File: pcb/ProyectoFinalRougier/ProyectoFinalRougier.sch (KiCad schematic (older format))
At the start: 24 parts, among them J1 Screw_Terminal_01x02, J2 Conn_01x06, J3 Screw_Terminal_01x02, U1 AD8495, U2 TL431DBZ, U3 AD8495, U4 TL431DBZ

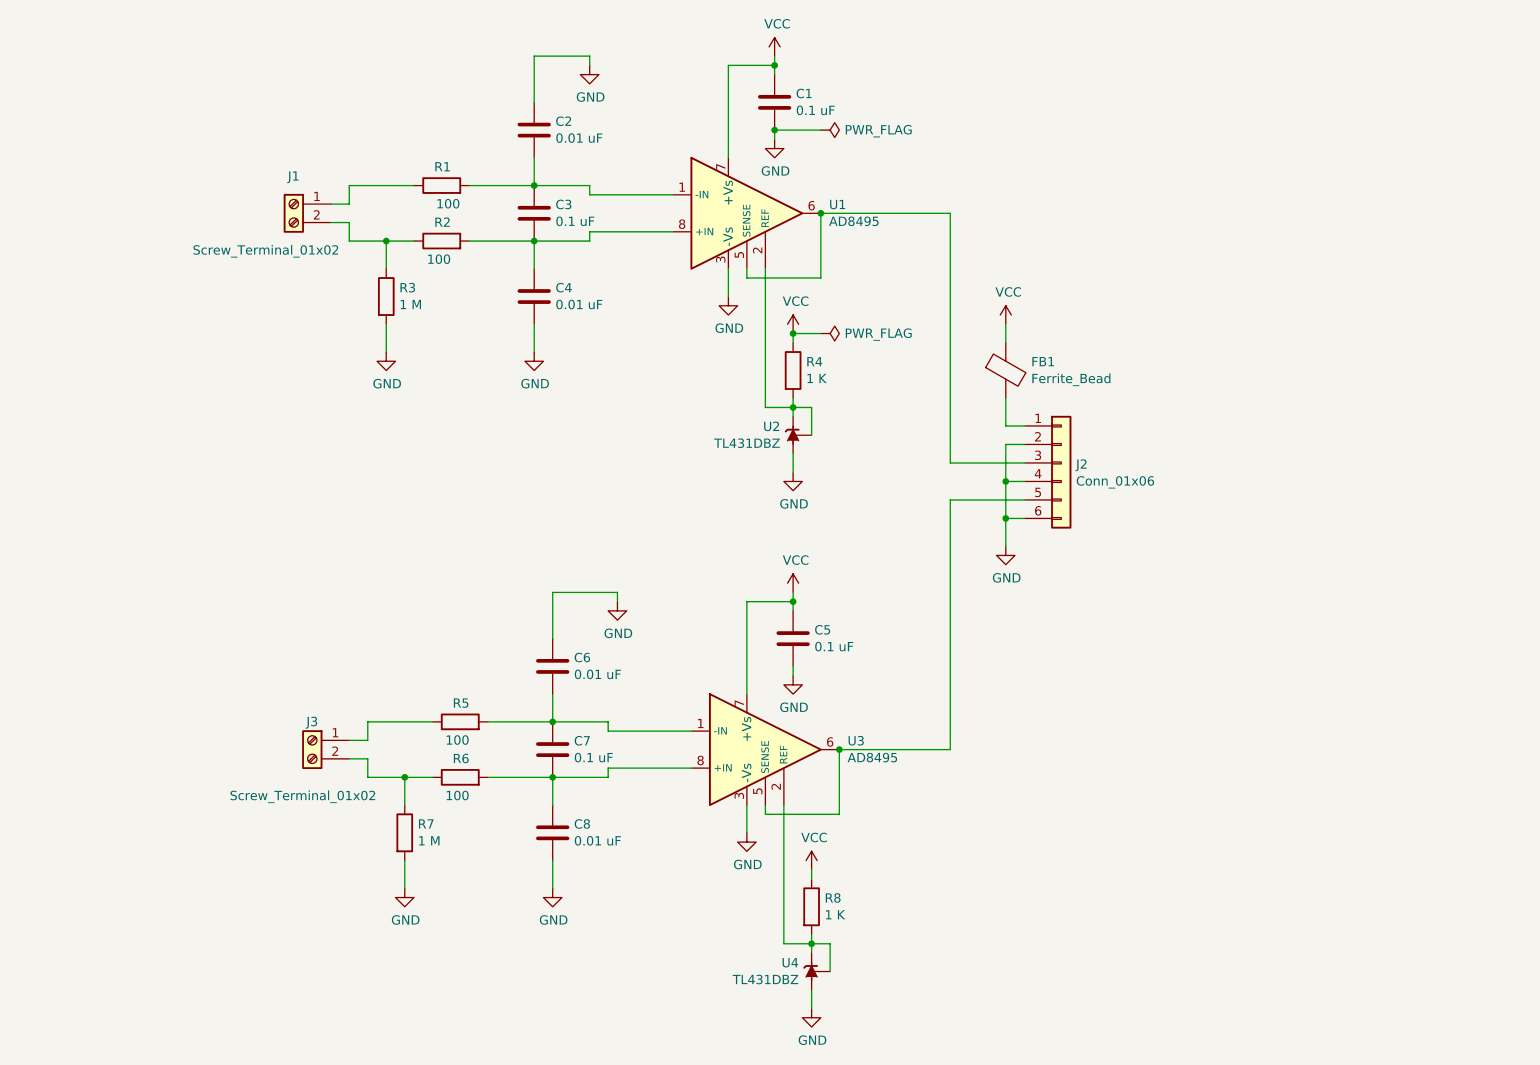
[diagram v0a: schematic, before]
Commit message: Se agregan Fiduciales y Mounting hole, se corrige ubicación de algunos componentes
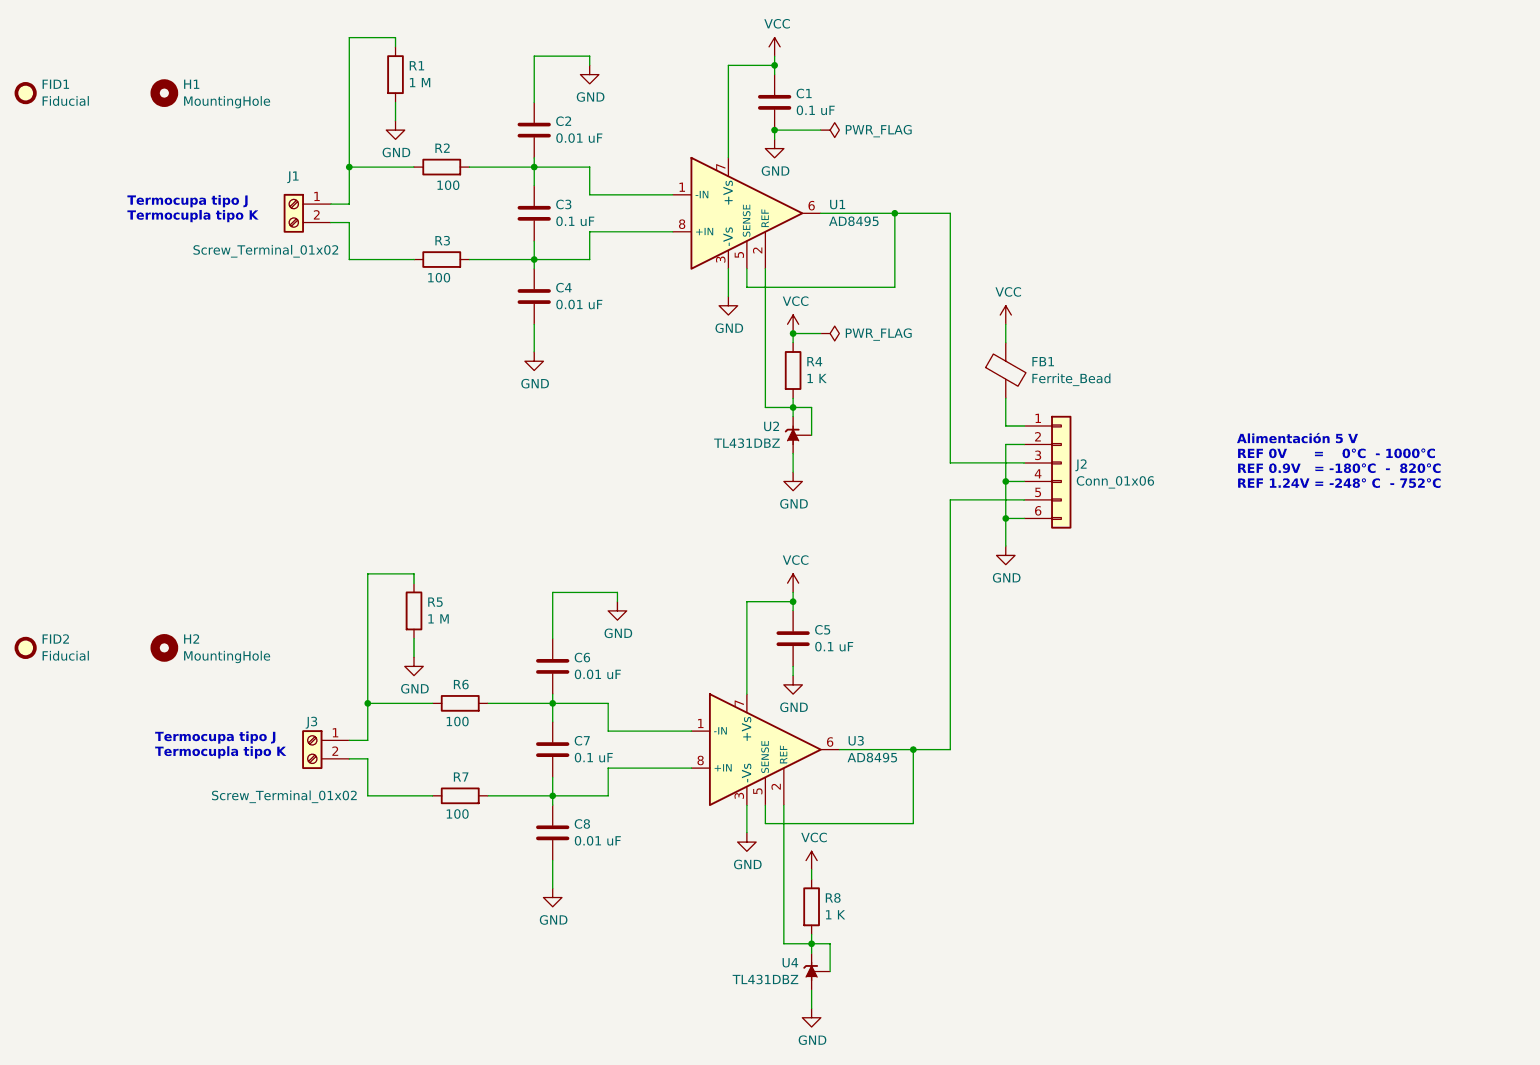
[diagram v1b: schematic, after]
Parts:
- added FID1, FID2: Fiducial, Fiducial:Fiducial_0.75mm_Mask2.25mm, symbol Mechanical:Fiducial
- added H1, H2: MountingHole, MountingHole:MountingHole_2.5mm, symbol Mechanical:MountingHole
- renumbered R3 to R1, R1 to R2, R2 to R3, R7 to R5, R5 to R6, R6 to R7
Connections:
- net at J1.2 (Pin_2), R3.1: no longer R1.1
- net at J1.1 (Pin_1), R2.1: now also R1.1
- net at J3.2 (Pin_2), R7.1: no longer R5.1
- net at J3.1 (Pin_1), R6.1: now also R5.1
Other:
- note added: "Alimentación 5 V\nREF 0V = 0°C - 1000°C\nREF 0.9V = -180°C - 820°C\nREF 1.24V = -248° C - 752°C"
- note added: "Termocupa tipo J\nTermocupla tipo K"
- moved on the sheet: R1, R2, R3, R5, R6, R7
